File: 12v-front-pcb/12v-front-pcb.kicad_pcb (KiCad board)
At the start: 2 copper layers, 231.1 x 146.1 mm, 48 parts

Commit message: Re-work front PCB
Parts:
- removed B1, B10, B2, B3, B4, B5, B6, B7, B8, B9: 282836-6, Socket:2828366
- removed BMS_RELAY1, HEADLIGHT_RELAY1, HIGHBEAM_RELAY1, INTERIOR_LIGHTS_RELAY1, LH_INDICATOR_RELAY1, RH_INDICATOR_RELAY1: DZ85AB-5-PCB, Socket:DZ85AB5PCB
- removed D10, D11, D12, D13, D14, D7, D8, D9: 10A10, Diode_THT:DIOAD1165W56L425D185
- removed FLASHER_FUSE1, HEADLIGHT_FUSE1, INTERIOR_LIGHTS_FUSE1: 178.6165.0001, Socket:17861650001
- added COOLANT_PUMP_RELAY1: DZ85AB-5-PCB, Connector:DZ85AB5PCB, F.Cu at (199.3, 211.0)
- added G***: LOGO, Symbol:mustang, F.Cu at (234.7, 87.7)
- added H5: MountingHole, MountingHole:MountingHole_3mm, F.Cu at (180.3, 133.3)
- added H6: MountingHole, MountingHole:MountingHole_3mm, F.Cu at (193.0, 194.3)
- added INVERTER_RELAY1: DZ85AB-5-PCB, Connector:DZ85AB5PCB, F.Cu at (135.6, 155.1)
- added J1: 172065-0208, Connector:1720650208, F.Cu at (193.0, 183.3)
- added J2: 172065-0208, Connector:1720650208, F.Cu at (134.6, 177.9)
- added J3: 172065-0208, Connector:1720650208, F.Cu at (229.7, 177.7)
- added J4: 172065-0208, Connector:1720650208, F.Cu at (212.3, 98.5)
- added RADIO_RELAY1: DZ85AB-5-PCB, Connector:DZ85AB5PCB, F.Cu at (236.2, 122.1)
- added VACUUM_RELAY1: DZ85AB-5-PCB, Connector:DZ85AB5PCB, F.Cu at (227.3, 155.1)
- DASHBOARD_RELAY1, FWD_DRIVE_INHIBIT_RELAY1, HORN_RELAY1, IGNITION_RELAY1, REV_DRIVE_INHIBIT_RELAY1: footprint Socket:DZ85AB5PCB -> Connector:DZ85AB5PCB
- moved H4 251.9 mm to (261.6, 219.7)
- moved H3 237.1 mm to (124.5, 219.7)
- moved DASHBOARD_RELAY1 148.2 mm to (232.3, 211.0)
- moved BMS_FUSE1 128.4 mm to (164.3, 176.6), turned to -90 degrees
- moved H1 111.3 mm to (124.5, 85.1)
- moved DASHBOARD_FUSE1 104.7 mm to (218.4, 174.1), turned to -90 degrees
- moved H2 103.6 mm to (261.6, 85.1)
- moved D2 97.7 mm to (162.6, 144.2), turned to -90 degrees
- moved D1 94.1 mm to (165.1, 144.2), turned to -90 degrees
- moved REV_DRIVE_INHIBIT_RELAY1 86.3 mm to (152.4, 211.0), turned to 180 degrees
- moved FWD_DRIVE_INHIBIT_RELAY1 83.6 mm to (185.4, 211.0), turned to 180 degrees
- moved COOLANT_PUMP_FUSE1 83.0 mm to (207.5, 174.1), turned to -90 degrees
- moved VACUUM_PUMP_FUSE1 73.4 mm to (229.8, 135.6)
- moved RADIO_FUSE1 54.6 mm to (210.1, 124.6), turned to 90 degrees
- moved INVERTER_FUSE1 50.9 mm to (209.3, 136.0), turned to 180 degrees
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- renumbered WATER_PUMP_FUSE1 to COOLANT_PUMP_FUSE1
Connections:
- net COOLANT_PUMP renamed Net-(COOLANT_PUMP_FUSE1-Pad3)
- net HVJB_12V renamed CONTACTORS_12V
- net INVERTER_12V renamed Net-(INVERTER_FUSE1-Pad3)
- net Net-(BMS_FUSE1-Pad3) renamed BMS_REAR_12V
- net RADIO_12V renamed Net-(RADIO_FUSE1-Pad3)
- net VACUUM_PUMP renamed Net-(VACUUM_PUMP_FUSE1-Pad3)
- BMS_FUSE1 pad 1: 12V_BATT -> IGNITION_SWITCH_A
- BMS_FUSE1 pad 2: Net-(BMS_FUSE1-Pad2) -> IGNITION_SWITCH_A
- BMS_FUSE1 pad 7: Net-(BMS_FUSE1-Pad7) -> IGNITION_SWITCH_A
- BMS_FUSE1 pad 8: 12V_BATT -> IGNITION_SWITCH_A
- COOLANT_PUMP_FUSE1 pad 1: BRAKE_SWITCH_A -> IGNITION_SWITCH_A
- COOLANT_PUMP_FUSE1 pad 2: BRAKE_SWITCH_A -> IGNITION_SWITCH_A
- COOLANT_PUMP_FUSE1 pad 7: BRAKE_SWITCH_A -> IGNITION_SWITCH_A
- COOLANT_PUMP_FUSE1 pad 8: BRAKE_SWITCH_A -> IGNITION_SWITCH_A
- D1 pad 1: Net-(D1-Pad1) -> IGN_OR_CHARGE
- D1 pad 2: BRAKE_SWITCH_A -> CRUISE_SWITCH_A
- D2 pad 1: Net-(D1-Pad1) -> IGN_OR_CHARGE
- DASHBOARD_FUSE1 pad 1: 12V_BATT -> IGNITION_SWITCH_A
- DASHBOARD_FUSE1 pad 2: 12V_BATT -> IGNITION_SWITCH_A
- DASHBOARD_FUSE1 pad 7: 12V_BATT -> IGNITION_SWITCH_A
- DASHBOARD_FUSE1 pad 8: 12V_BATT -> IGNITION_SWITCH_A
- DASHBOARD_RELAY1 pad 1: Net-(DASHBOARD_FUSE1-Pad3) -> DASHBOARD_12V
- DASHBOARD_RELAY1 pad 2: Net-(DASHBOARD_RELAY1-Pad2) -> unconnected-(DASHBOARD_RELAY1-Pad2)
- DASHBOARD_RELAY1 pad 3: DASHBOARD_12V -> Net-(DASHBOARD_FUSE1-Pad3)
- DASHBOARD_RELAY1 pad 4: BMS_GND -> IGN_OR_CHARGE
- DASHBOARD_RELAY1 pad 5: Net-(D1-Pad1) -> BMS_FRONT_GND
- FWD_DRIVE_INHIBIT_RELAY1 pad 1: SHIFTER_FWD -> unconnected-(FWD_DRIVE_INHIBIT_RELAY1-Pad1)
- FWD_DRIVE_INHIBIT_RELAY1 pad 3: Net-(FWD_DRIVE_INHIBIT_RELAY1-Pad3) -> SHIFTER_FWD
- FWD_DRIVE_INHIBIT_RELAY1 pad 4: BMS_GND -> DRIVE_INHIBIT
- FWD_DRIVE_INHIBIT_RELAY1 pad 5: DRIVE_INHIBIT -> BMS_FRONT_GND
- HEATER_FAN_FUSE1 pad 1: BRAKE_SWITCH_A -> CRUISE_SWITCH_A
- HEATER_FAN_FUSE1 pad 2: BRAKE_SWITCH_A -> CRUISE_SWITCH_A
- HEATER_FAN_FUSE1 pad 7: BRAKE_SWITCH_A -> CRUISE_SWITCH_A
- HEATER_FAN_FUSE1 pad 8: BRAKE_SWITCH_A -> CRUISE_SWITCH_A
- HORN_FUSE1 pad 1: BRAKE_SWITCH_A -> CRUISE_SWITCH_A
- HORN_FUSE1 pad 2: BRAKE_SWITCH_A -> CRUISE_SWITCH_A
- HORN_FUSE1 pad 7: BRAKE_SWITCH_A -> CRUISE_SWITCH_A
- HORN_FUSE1 pad 8: BRAKE_SWITCH_A -> CRUISE_SWITCH_A
- HORN_RELAY1 pad 1: Net-(HORN_FUSE1-Pad3) -> HORN
- HORN_RELAY1 pad 2: Net-(HORN_RELAY1-Pad2) -> unconnected-(HORN_RELAY1-Pad2)
- HORN_RELAY1 pad 3: HORN -> Net-(HORN_FUSE1-Pad3)
- HORN_RELAY1 pad 4: BMS_GND -> HORN_SWITCH_B
- HORN_RELAY1 pad 5: HORN_SWITCH_B -> BMS_FRONT_GND
- HVJB_FUSE1 pad 1: BRAKE_SWITCH_A -> CRUISE_SWITCH_A
- HVJB_FUSE1 pad 2: BRAKE_SWITCH_A -> CRUISE_SWITCH_A
- HVJB_FUSE1 pad 7: BRAKE_SWITCH_A -> CRUISE_SWITCH_A
- HVJB_FUSE1 pad 8: BRAKE_SWITCH_A -> CRUISE_SWITCH_A
- IGNITION_FUSE1 pad 3: Net-(IGNITION_FUSE1-Pad3) -> IGNITION_SWITCH_A
- IGNITION_FUSE1 pad 4: Net-(IGNITION_FUSE1-Pad3) -> IGNITION_SWITCH_A
- IGNITION_FUSE1 pad 5: Net-(IGNITION_FUSE1-Pad3) -> IGNITION_SWITCH_A
- IGNITION_FUSE1 pad 6: Net-(IGNITION_FUSE1-Pad3) -> IGNITION_SWITCH_A
- IGNITION_RELAY1 pad 1: Net-(IGNITION_FUSE1-Pad3) -> CRUISE_SWITCH_A
- IGNITION_RELAY1 pad 2: Net-(IGNITION_RELAY1-Pad2) -> unconnected-(IGNITION_RELAY1-Pad2)
- IGNITION_RELAY1 pad 3: BRAKE_SWITCH_A -> IGNITION_SWITCH_A
- IGNITION_RELAY1 pad 4: BMS_GND -> IGNITION_SWITCH_B
- IGNITION_RELAY1 pad 5: IGNITION_SWITCH_B -> BMS_FRONT_GND
- INVERTER_FUSE1 pad 1: BRAKE_SWITCH_A -> IGNITION_SWITCH_A
- INVERTER_FUSE1 pad 2: BRAKE_SWITCH_A -> IGNITION_SWITCH_A
- INVERTER_FUSE1 pad 7: BRAKE_SWITCH_A -> IGNITION_SWITCH_A
- INVERTER_FUSE1 pad 8: BRAKE_SWITCH_A -> IGNITION_SWITCH_A
- RADIO_FUSE1 pad 1: BRAKE_SWITCH_A -> IGNITION_SWITCH_A
- RADIO_FUSE1 pad 2: BRAKE_SWITCH_A -> IGNITION_SWITCH_A
- RADIO_FUSE1 pad 7: BRAKE_SWITCH_A -> IGNITION_SWITCH_A
- RADIO_FUSE1 pad 8: BRAKE_SWITCH_A -> IGNITION_SWITCH_A
- REV_DRIVE_INHIBIT_RELAY1 pad 1: SHIFTER_REV -> unconnected-(REV_DRIVE_INHIBIT_RELAY1-Pad1)
- REV_DRIVE_INHIBIT_RELAY1 pad 3: Net-(REV_DRIVE_INHIBIT_RELAY1-Pad3) -> SHIFTER_REV
- REV_DRIVE_INHIBIT_RELAY1 pad 4: BMS_GND -> DRIVE_INHIBIT
- REV_DRIVE_INHIBIT_RELAY1 pad 5: DRIVE_INHIBIT -> BMS_FRONT_GND
- VACUUM_PUMP_FUSE1 pad 1: BRAKE_SWITCH_A -> IGNITION_SWITCH_A
- VACUUM_PUMP_FUSE1 pad 2: BRAKE_SWITCH_A -> IGNITION_SWITCH_A
- VACUUM_PUMP_FUSE1 pad 7: BRAKE_SWITCH_A -> IGNITION_SWITCH_A
- VACUUM_PUMP_FUSE1 pad 8: BRAKE_SWITCH_A -> IGNITION_SWITCH_A
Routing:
- net BMS_GND: track 740.9 -> 0.00 mm
- net BRAKE_SWITCH_A: track 459.2 -> 0.00 mm, vias 1 -> 0
- net BMS_FRONT_GND: track 0.00 -> 455.8 mm
- net 12V_BATT: track 394.7 -> 25.7 mm
- net CRUISE_SWITCH_A: track 0.00 -> 237.8 mm
- net IGNITION_SWITCH_A: track 0.00 -> 169.5 mm
- net IGN_OR_CHARGE: track 0.00 -> 153.0 mm
- net CONTACTORS_12V: track 152.5 -> 21.6 mm
- net Net-(VACUUM_PUMP_FUSE1-Pad3): track 137.2 -> 20.6 mm
- net Net-(RADIO_FUSE1-Pad3): track 145.1 -> 31.8 mm
- net HEATER_FAN_12V: track 130.9 -> 19.6 mm
- net INTERIOR_LIGHTS: track 111.0 -> 0.00 mm
- net INTERIOR_LIGHT_SWITCH_B: track 109.7 -> 0.00 mm
- net INVERTER_12V: track 0.00 -> 99.1 mm
- net RH_INDICATOR: track 82.3 -> 0.00 mm
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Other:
- board outline removed
- net class Default removed
- board text added: "CABIN HEATER"
- board text added: "CONTACTOR"
- board text added: "ELECTRIC MUSTANG Low voltage system - engine Version 2"
- board text removed: "12V BATT"
- board text removed: "BMS 12V"
- board text removed: "BMS GND"
- board text removed: "BRAKE SW A"
- board text removed: "CHARGER ON"
- board text removed: "DASH 12V"
- board text removed: "DASH GND"
- board text removed: "DASH HI IND"
- board text removed: "DASH IND IND"
- board text removed: "DRIVE INHIBIT"
- board text removed: "EV MUSTANG Low voltage system Version 1.0"
- board text removed: "FLASHER"
- board text removed: "FLASHER A"
- board text removed: "GND"
- board text removed: "HAZ SW A"
- board text removed: "HAZARD SW B"
- board text removed: "HEAD SW A"
- board text removed: "HEADL SW B"
- board text removed: "HEADLIGHT"
- board text removed: "HEATER"
- board text removed: "HEATER FAN"
- board text removed: "HI A"
- board text removed: "HI SW"
- board text removed: "HIGHBEAM"
- board text removed: "HL"
- board text removed: "HORN A"
- board text removed: "HORN SW B"
- board text removed: "HVJB"
- board text removed: "HVJB 12V"
- board text removed: "HVJB GND"
- board text removed: "IGN"
- board text removed: "IGN SW"
- board text removed: "IGN SW A"
- board text removed: "INT LIGHTS"
- board text removed: "INT SW A"
- board text removed: "INT SW B"
- board text removed: "INV 12V"
- board text removed: "INV FWD"
- board text removed: "INV GND"
- board text removed: "INV REV"
- board text removed: "LH F IND"
- board text removed: "LH IND"
- board text removed: "LH IND A"
- board text removed: "LH IND SW B"
- board text removed: "PERM 12V"
- board text removed: "REV SIG"
- board text removed: "RH F IND"
- board text removed: "RH IND"
- board text removed: "RH IND A"
- board text removed: "RH IND SW B"
- board text removed: "SHIFTER 12V"
- board text removed: "SHIFTER FWD"
- board text removed: "SHIFTER REV"
- board text removed: "—"

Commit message: 12v front board
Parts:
- moved H6 3.59 mm to (195.6, 191.8)
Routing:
- net IGNITION_SWITCH_A: track 169.5 -> 241.0 mm
- net CRUISE_SWITCH_A: track 237.8 -> 266.3 mm
- net Net-(COOLANT_PUMP_FUSE1-Pad3): track 27.1 -> 39.1 mm
- net Net-(VACUUM_PUMP_FUSE1-Pad3): track 20.6 -> 32.6 mm
- net Net-(DASHBOARD_FUSE1-Pad3): track 47.4 -> 59.4 mm
- net BMS_REAR_12V: track 32.5 -> 44.5 mm
- net Net-(RADIO_FUSE1-Pad3): track 31.8 -> 41.3 mm
- net Net-(HORN_FUSE1-Pad3): track 27.6 -> 37.1 mm
- net HEATER_FAN_12V: track 19.6 -> 29.1 mm
- net CONTACTORS_12V: track 21.6 -> 31.1 mm
- net 12V_BATT: track 25.7 -> 35.2 mm
- net Net-(INVERTER_FUSE1-Pad3): track 55.3 -> 64.8 mm
- net VACUUM_PUMP: track 32.6 -> 38.2 mm
- net BMS_FRONT_GND: track 455.8 -> 458.1 mm

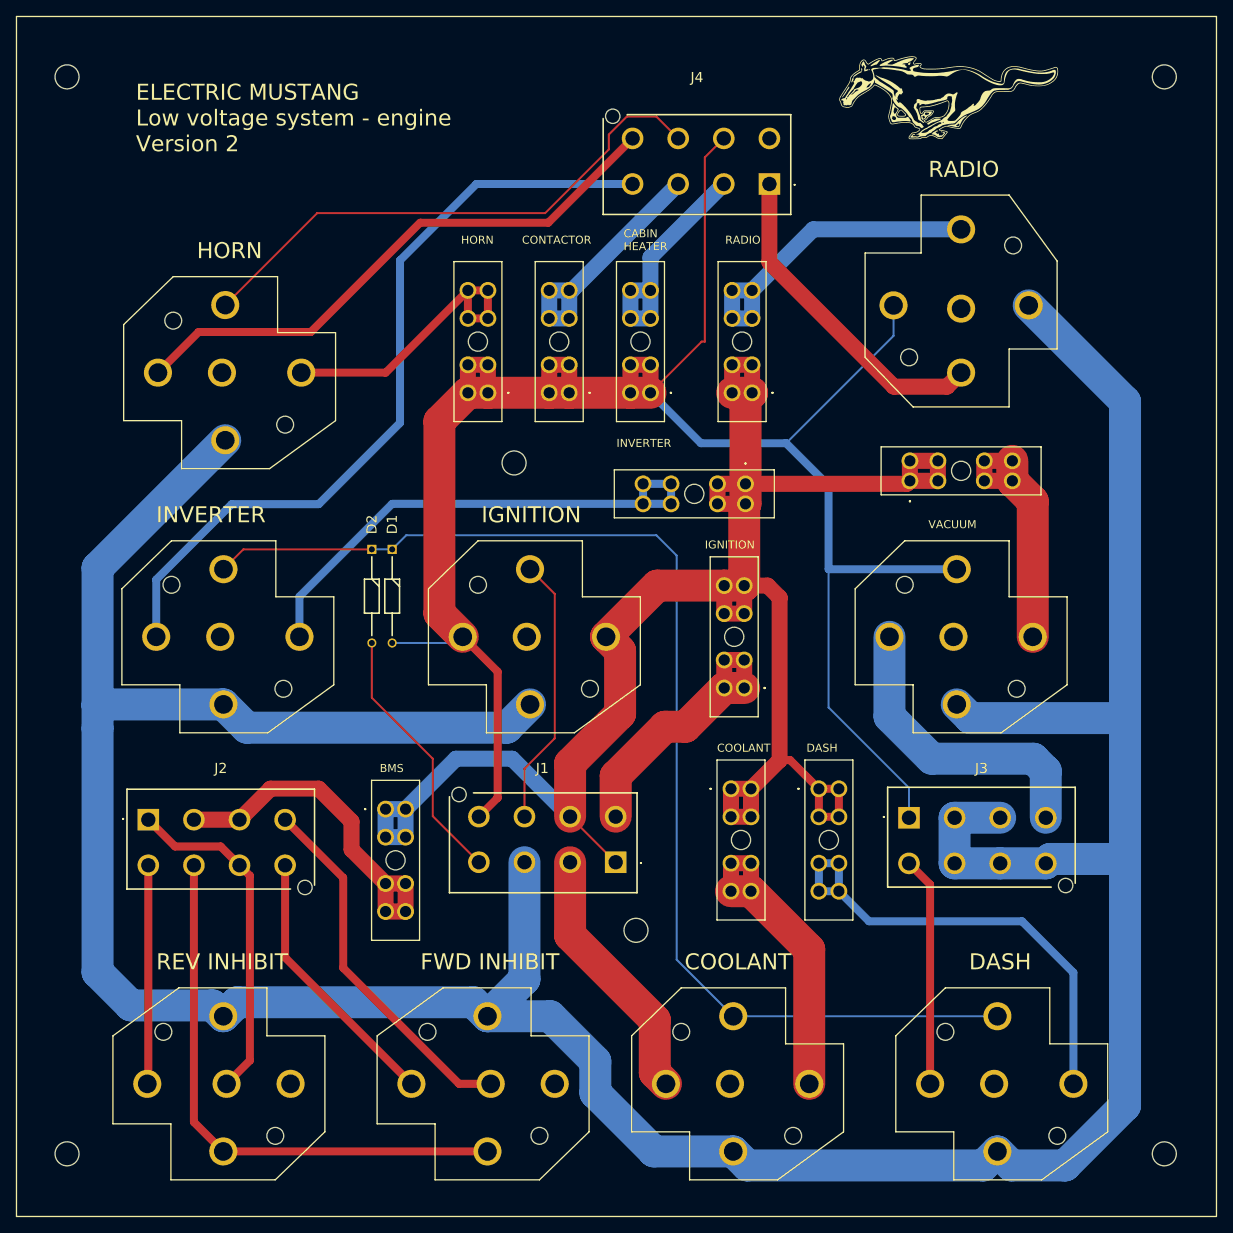
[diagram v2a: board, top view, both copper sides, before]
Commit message: Finalised 12v front PCB design (engine board) and sent for fabrication
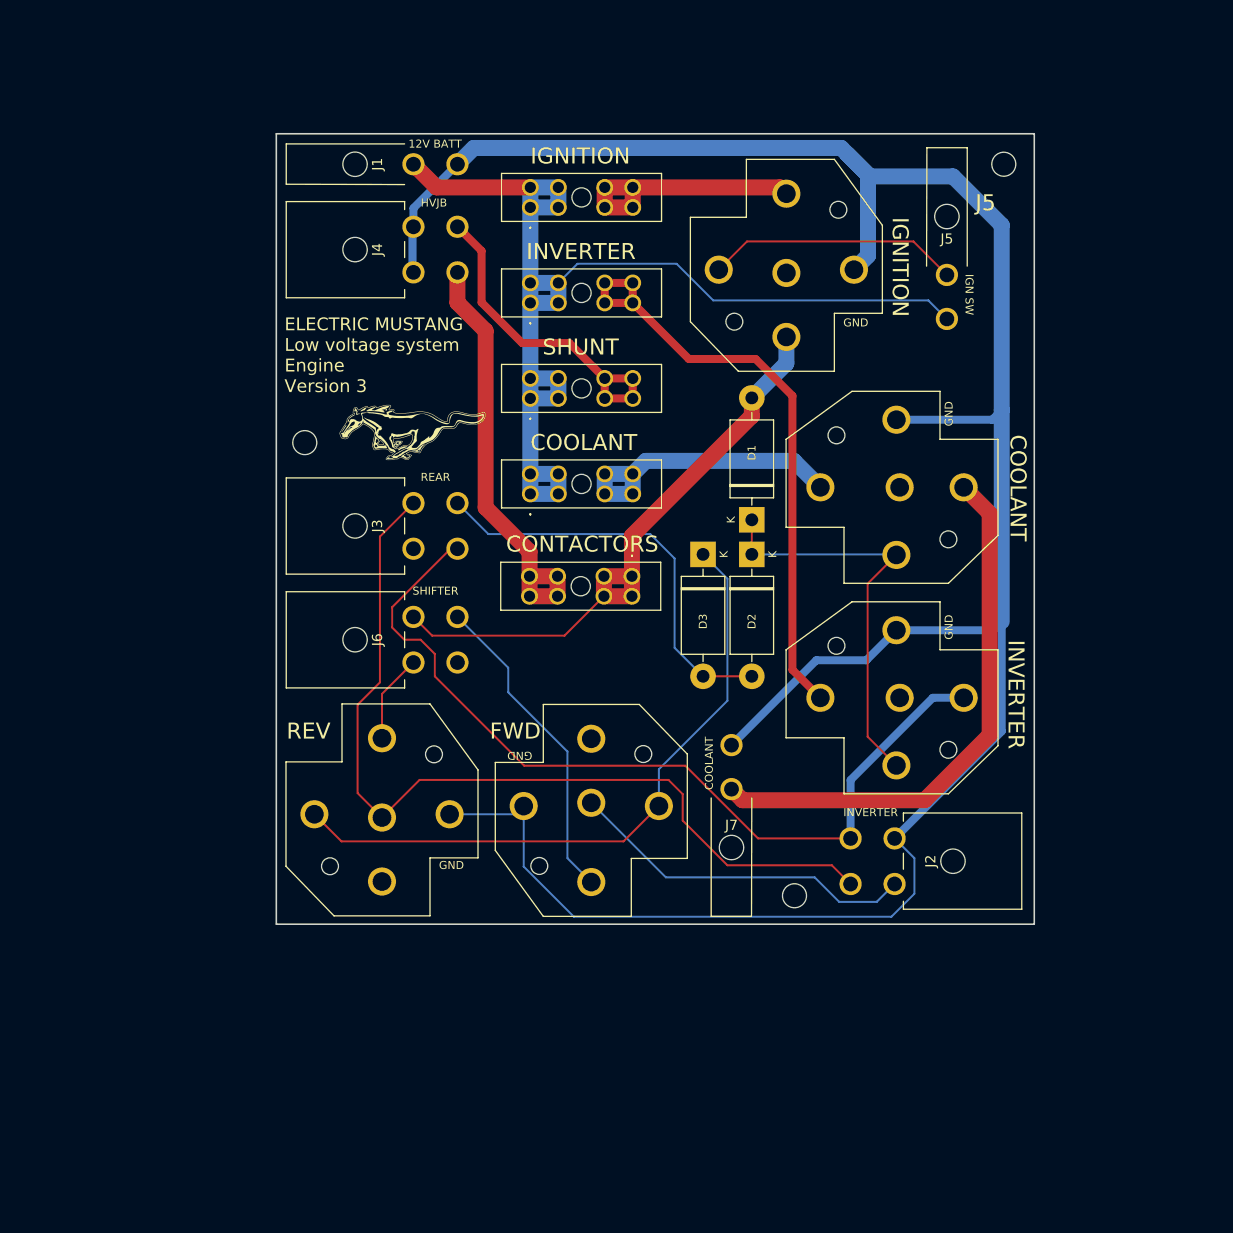
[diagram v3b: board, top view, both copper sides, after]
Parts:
- removed BMS_FUSE1, DASHBOARD_FUSE1, HEATER_FAN_FUSE1, HORN_FUSE1, HVJB_FUSE1, RADIO_FUSE1, VACUUM_PUMP_FUSE1: 178.6165.0001, Socket:17861650001
- removed DASHBOARD_RELAY1, HORN_RELAY1, RADIO_RELAY1, VACUUM_RELAY1: DZ85AB-5-PCB, Connector:DZ85AB5PCB
- removed the G*** at (234.7, 87.7)
- removed H1, H5, H6: MountingHole, MountingHole:MountingHole_3mm
- added CONTACTORS_FUSE1: 178.6165.0001, Socket:17861650001, F.Cu at (195.1, 147.5)
- added D3: 1N5406, Diode_THT:D_DO-201AD_P15.24mm_Horizontal, F.Cu at (204.0, 144.8)
- added G***: LOGO, LOGO, F.Cu at (167.6, 129.5)
- added ISA_SHUNT_FUSE1: 178.6165.0001, Socket:17861650001, F.Cu at (182.4, 125.3)
- added J5: 76825-0002, Connector:768250002, F.Cu at (234.4, 104.6)
- added J6: 76825-0004, Connector:768250004, F.Cu at (162.6, 155.4)
- added J7: 76825-0002, Connector:768250002, F.Cu at (207.5, 179.3)
- D1, D2: value 10A10 -> 1N5406; footprint Diode_THT:DIOAD1165W56L425D185 -> Diode_THT:D_DO-201AD_P15.24mm_Horizontal
- J1: value 172065-0208 -> 76825-0002; footprint Connector:1720650208 -> Connector:768250002
- J2, J3, J4: value 172065-0208 -> 76825-0004; footprint Connector:1720650208 -> Connector:768250004
- moved INVERTER_RELAY1 101.2 mm to (236.5, 162.7), turned to 180 degrees
- moved J2 98.6 mm to (233.1, 183.1), turned to 90 degrees
- moved H3 93.7 mm to (154.2, 130.8)
- moved J1 92.4 mm to (162.6, 96.0), turned to -90 degrees
- moved COOLANT_PUMP_RELAY1 83.3 mm to (236.5, 136.4), turned to 180 degrees
- moved J3 76.4 mm to (162.6, 141.2), turned to -90 degrees
- moved IGNITION_FUSE1 65.8 mm to (182.4, 101.4), turned to 0 degrees
- moved H4 56.4 mm to (215.4, 187.5)
- moved IGNITION_RELAY1 55.1 mm to (214.4, 117.6), turned to 90 degrees
- moved J4 50.4 mm to (162.6, 106.7), turned to -90 degrees
- moved D2 47.5 mm to (210.1, 144.8)
- moved D1 45.1 mm to (210.1, 140.5), turned to 90 degrees
- moved COOLANT_PUMP_FUSE1 44.6 mm to (182.4, 137.2), turned to 0 degrees
- moved FWD_DRIVE_INHIBIT_RELAY1 43.4 mm to (190.0, 167.8), turned to -90 degrees
- moved INVERTER_FUSE1 35.1 mm to (182.4, 113.3), turned to 0 degrees
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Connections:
- net IGN_OR_CHARGE renamed Net-(COOLANT_PUMP_RELAY1-Pad4)
- COOLANT_PUMP_FUSE1 pad 1: IGNITION_SWITCH_A -> 12V_BATT_IN
- COOLANT_PUMP_FUSE1 pad 2: IGNITION_SWITCH_A -> 12V_BATT_IN
- COOLANT_PUMP_FUSE1 pad 7: IGNITION_SWITCH_A -> 12V_BATT_IN
- COOLANT_PUMP_FUSE1 pad 8: IGNITION_SWITCH_A -> 12V_BATT_IN
- COOLANT_PUMP_RELAY1 pad 1: COOLANT_PUMP -> COOLANT_12V
- COOLANT_PUMP_RELAY1 pad 5: BMS_FRONT_GND -> CONTACTORS_GND
- D1 pad 2: CRUISE_SWITCH_A -> IGNITION_12V
- D2 pad 2: CHARGER_ON_SIGNAL -> CHARGER_ENABLE_IN
- FWD_DRIVE_INHIBIT_RELAY1 pad 4: DRIVE_INHIBIT -> Net-(FWD_DRIVE_INHIBIT_RELAY1-Pad4)
- FWD_DRIVE_INHIBIT_RELAY1 pad 5: BMS_FRONT_GND -> CONTACTORS_GND
- IGNITION_FUSE1 pad 1: 12V_BATT -> 12V_BATT_IN
- IGNITION_FUSE1 pad 2: 12V_BATT -> 12V_BATT_IN
- IGNITION_FUSE1 pad 3: IGNITION_SWITCH_A -> Net-(IGNITION_FUSE1-Pad3)
- IGNITION_FUSE1 pad 4: IGNITION_SWITCH_A -> Net-(IGNITION_FUSE1-Pad3)
- IGNITION_FUSE1 pad 5: IGNITION_SWITCH_A -> Net-(IGNITION_FUSE1-Pad3)
- IGNITION_FUSE1 pad 6: IGNITION_SWITCH_A -> Net-(IGNITION_FUSE1-Pad3)
- IGNITION_FUSE1 pad 7: 12V_BATT -> 12V_BATT_IN
- IGNITION_FUSE1 pad 8: 12V_BATT -> 12V_BATT_IN
- IGNITION_RELAY1 pad 1: CRUISE_SWITCH_A -> IGNITION_12V
- IGNITION_RELAY1 pad 3: IGNITION_SWITCH_A -> Net-(IGNITION_FUSE1-Pad3)
- IGNITION_RELAY1 pad 5: BMS_FRONT_GND -> CONTACTORS_GND
- INVERTER_FUSE1 pad 1: IGNITION_SWITCH_A -> 12V_BATT_IN
- INVERTER_FUSE1 pad 2: IGNITION_SWITCH_A -> 12V_BATT_IN
- INVERTER_FUSE1 pad 7: IGNITION_SWITCH_A -> 12V_BATT_IN
- INVERTER_FUSE1 pad 8: IGNITION_SWITCH_A -> 12V_BATT_IN
- INVERTER_RELAY1 pad 5: BMS_FRONT_GND -> CONTACTORS_GND
- J1 pad 1: IGNITION_SWITCH_A -> CONTACTORS_GND
- J1 pad 2: COOLANT_PUMP -> 12V_BATT_IN
- J2 pad 2: BMS_REAR_12V -> INVERTER_12V
- J2 pad 3: BMS_REAR_12V -> INVERTER_FWD
- J2 pad 4: INVERTER_FWD -> CONTACTORS_GND
- J3 pad 1: CRUISE_SWITCH_A -> CHARGER_ENABLE_IN
- J3 pad 2: BMS_FRONT_GND -> INVERTER_12V
- J3 pad 3: BMS_FRONT_GND -> INVERTER_REV
- J3 pad 4: VACUUM_PUMP -> unconnected-(J3-Pad4)
- J4 pad 1: RADIO_12V -> ISA_SHUNT_12V
- J4 pad 2: HEATER_FAN_12V -> CONTACTORS_12V
- J4 pad 3: CONTACTORS_12V -> CONTACTORS_GND
- J4 pad 4: INVERTER_12V -> CONTACTORS_GND
- REV_DRIVE_INHIBIT_RELAY1 pad 4: DRIVE_INHIBIT -> Net-(FWD_DRIVE_INHIBIT_RELAY1-Pad4)
- REV_DRIVE_INHIBIT_RELAY1 pad 5: BMS_FRONT_GND -> CONTACTORS_GND
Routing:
- net BMS_FRONT_GND: track 458.1 -> 0.00 mm
- net CONTACTORS_GND: track 0.00 -> 318.8 mm
- net CRUISE_SWITCH_A: track 266.3 -> 0.00 mm
- net IGNITION_SWITCH_A: track 241.0 -> 0.00 mm
- net 12V_BATT_IN: track 0.00 -> 144.2 mm
- net Net-(COOLANT_PUMP_RELAY1-Pad4): track 153.0 -> 51.7 mm
- net Net-(FWD_DRIVE_INHIBIT_RELAY1-Pad4): track 0.00 -> 82.6 mm
- net IGNITION_12V: track 0.00 -> 76.7 mm
- net HORN: track 71.5 -> 0.00 mm
- net DRIVE_INHIBIT: track 70.3 -> 0.00 mm
- net HORN_SWITCH_B: track 68.6 -> 0.00 mm
- net COOLANT_12V: track 0.00 -> 68.5 mm
- net INVERTER_REV: track 42.8 -> 111.3 mm
- net Net-(DASHBOARD_FUSE1-Pad3): track 59.4 -> 0.00 mm
- net CHARGER_ENABLE_IN: track 0.00 -> 52.3 mm
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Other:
- board outline added: 94.7 x 98.8 mm
- board text added: "12V BATT"
- board text added: "CONTACTORS"
- board text added: "ELECTRIC MUSTANG Low voltage system Engine Version 3"
- board text added: "FWD"
- board text added: "GND"
- board text added: "HVJB"
- board text added: "IGN SW"
- board text added: "J5"
- board text added: "REAR"
- board text added: "REV"
- board text added: "SHIFTER"
- board text added: "SHUNT"
- board text removed: "BMS"
- board text removed: "CABIN HEATER"
- board text removed: "CONTACTOR"
- board text removed: "DASH"
- board text removed: "ELECTRIC MUSTANG Low voltage system - engine Version 2"
- board text removed: "FWD INHIBIT"
- board text removed: "HORN"
- board text removed: "RADIO"
- board text removed: "REV INHIBIT"
- board text removed: "VACUUM"
